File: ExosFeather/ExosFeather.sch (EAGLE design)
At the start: 12 parts, among them J2 TC_2050_IDC_TOP, J6 CONN_2X1_JST_PA, U1 MCP73831, U2 STM32L052KX

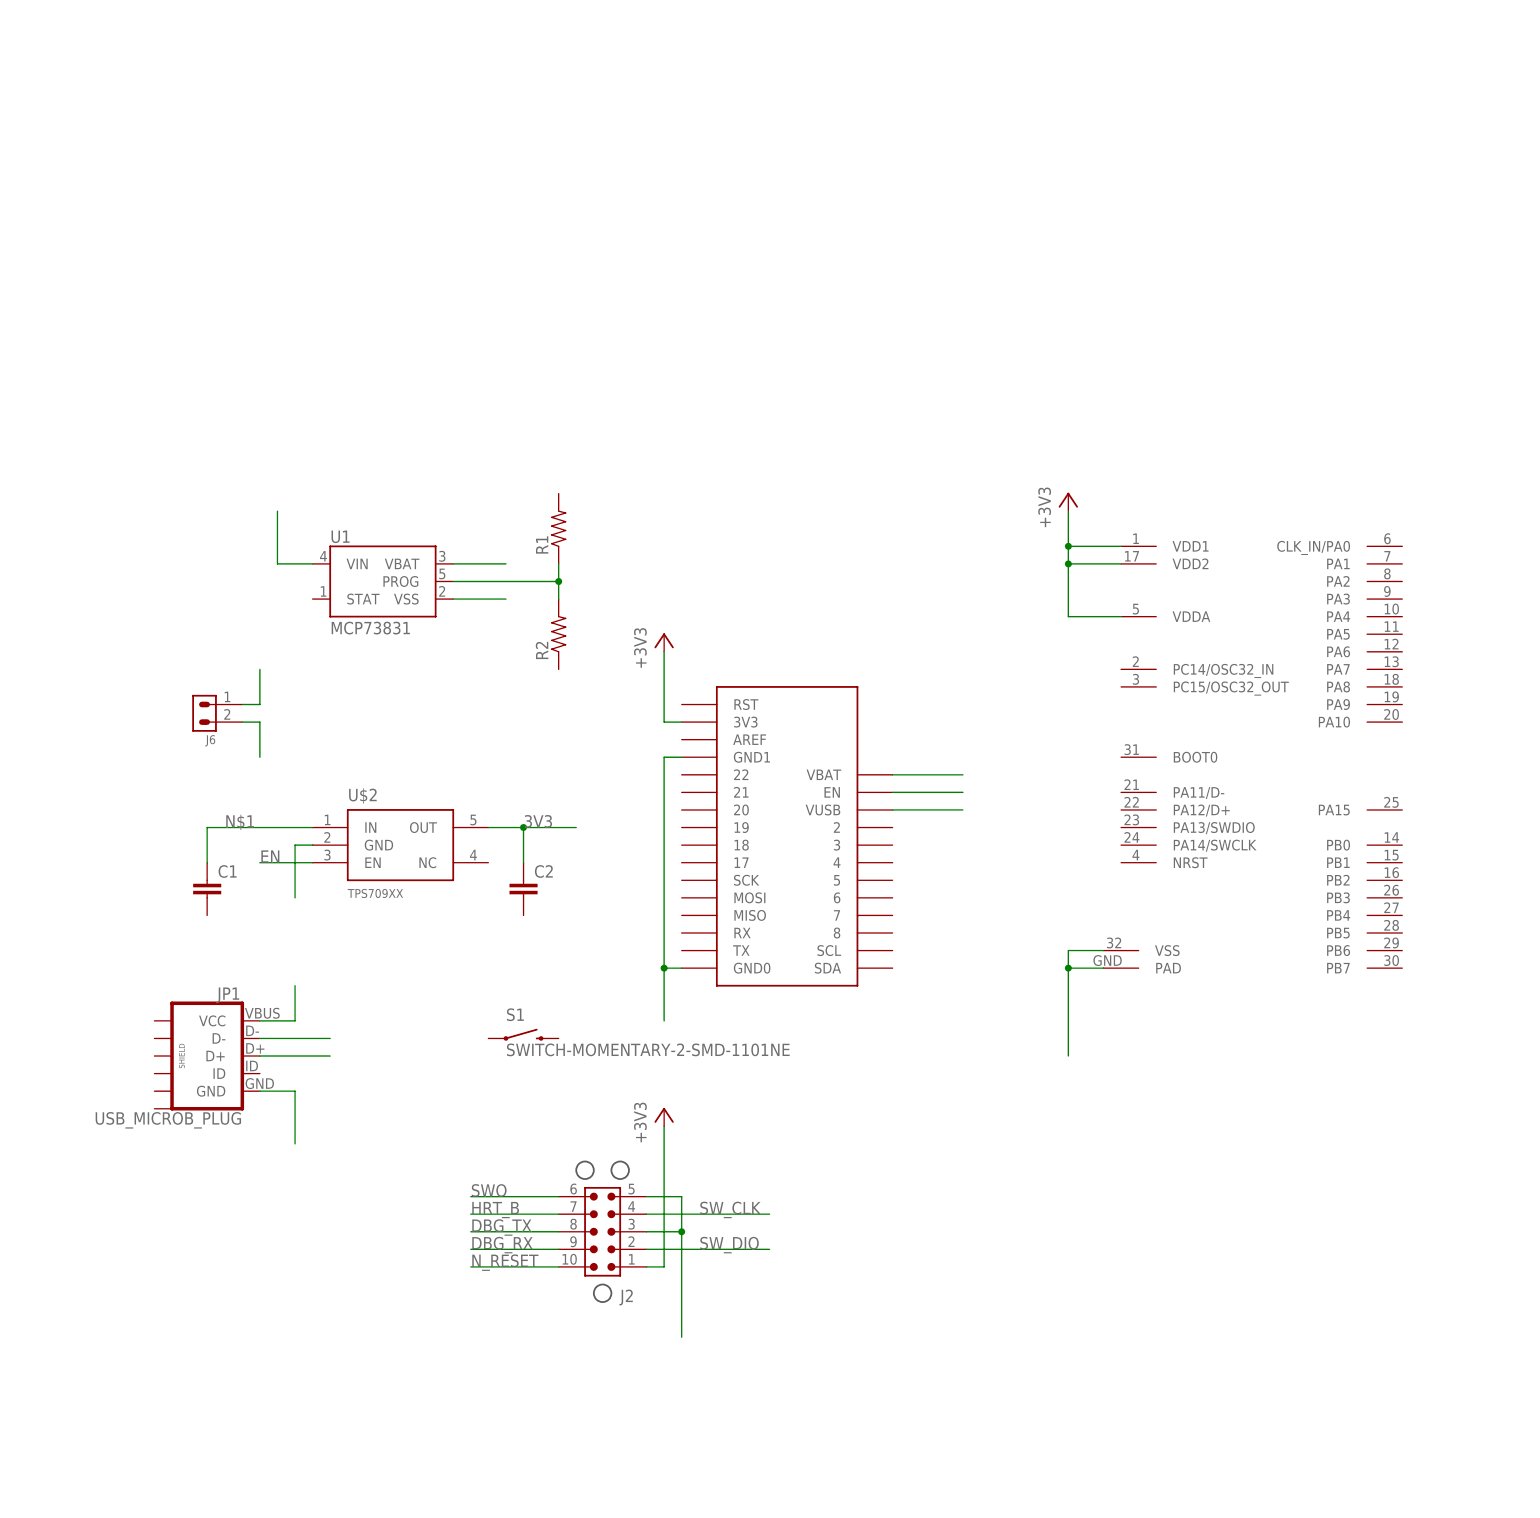
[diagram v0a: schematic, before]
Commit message: exosfeather
updated the pinouts
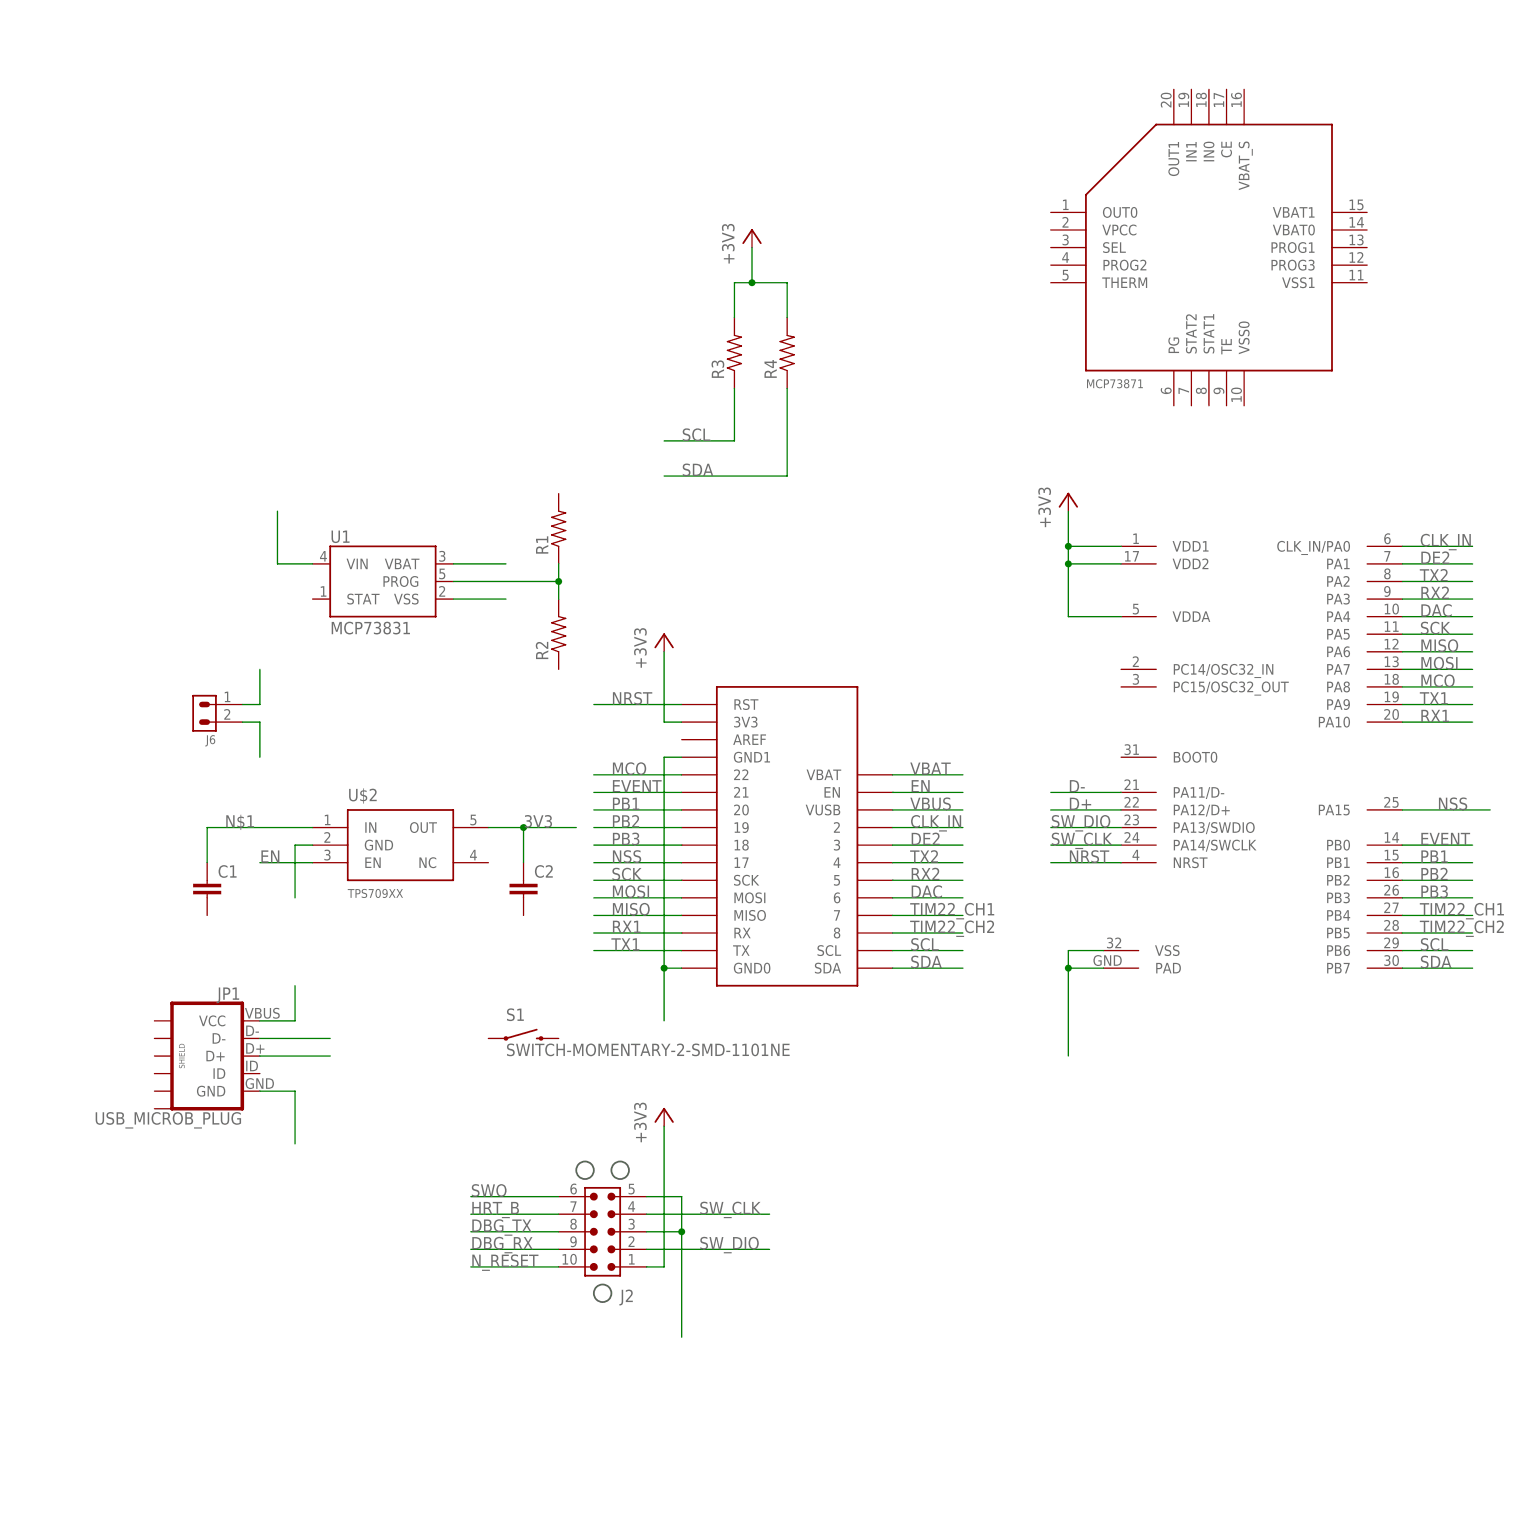
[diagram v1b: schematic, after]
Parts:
- added R3, R4: (no value), stepOSP:0603_RES
- added U$3: MCP73871, stepOSP:MCP73871
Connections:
- new net CLK_IN: U$1.2, U2.CLK_IN/PA0
- new net DAC: U$1.6, U2.PA4
- new net DE2: U$1.3, U2.PA1
- new net EVENT: U$1.21, U2.PB0
- new net MCO: U$1.22, U2.PA8
- new net MISO: U$1.MISO, U2.PA6
- new net MOSI: U$1.MOSI, U2.PA7
- new net NRST: U$1.RST, U2.NRST
- new net NSS: U$1.17, U2.PA15
- new net PB1: U$1.20, U2.PB1
- new net PB2: U$1.19, U2.PB2
- new net PB3: U$1.18, U2.PB3
- new net RX1: U$1.RX, U2.PA10
- new net RX2: U$1.5, U2.PA3
- new net SCK: U$1.SCK, U2.PA5
- new net SCL: R3.1, U$1.SCL, U2.PB6
- new net SDA: R4.1, U$1.SDA, U2.PB7
- new net TIM22_CH1: U$1.7, U2.PB4
- new net TIM22_CH2: U$1.8, U2.PB5
- new net TX1: U$1.TX, U2.PA9
- new net TX2: U$1.4, U2.PA2
- net +3V3: now also R3.2, R4.2
- net D+: now also U2.PA12/D+
- net D-: now also U2.PA11/D-
- net SW_CLK: now also U2.PA14/SWCLK
- net SW_DIO: now also U2.PA13/SWDIO

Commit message: exosfeather
added some new parts
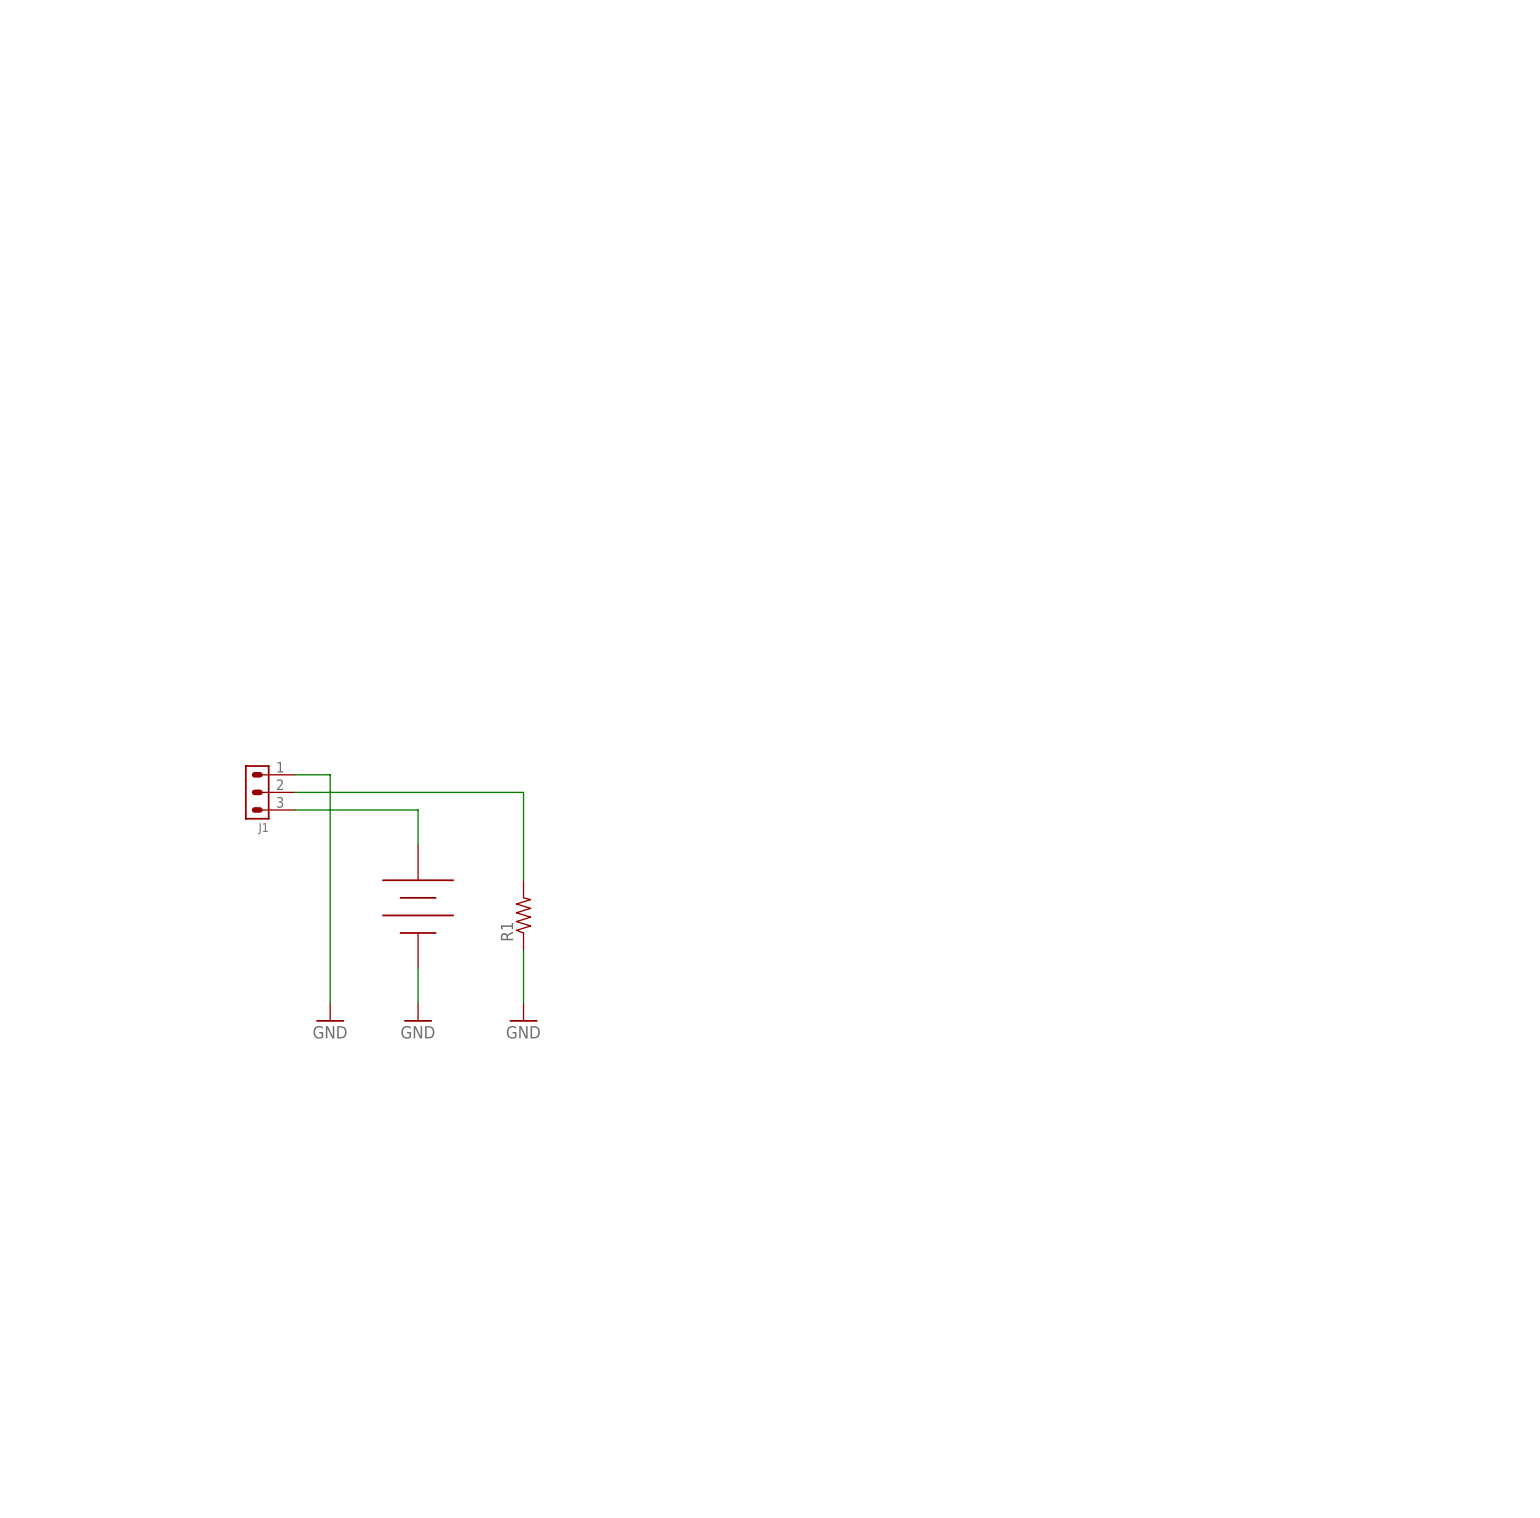
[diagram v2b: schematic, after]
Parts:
- removed C1, C2: (no value), stepOSP:0603_CAP
- removed J2: TC_2050_IDC_TOP, leaf:TC_2050_IDC_TOP
- removed J6: CONN_2X1_JST_PA, leaf:CONN_2X1_JST_PA
- removed JP1: USB_MICROB_PLUG, stepOSP:USB_MICROB_PLUG
- removed R2, R3, R4: (no value), stepOSP:0603_RES
- removed S1: SWITCH-MOMENTARY-2-SMD-1101NE, SparkFun-Electromechanical:SWITCH-MOMENTARY-2-SMD-1101NE
- removed U$1: FEATHER_PINOUT_FULL, stepOSP:FEATHER_PINOUT_FULL
- removed U$3: MCP73871, stepOSP:MCP73871
- removed U1: MCP73831, SparkFun-PowerIC:MCP73831
- removed U2: STM32L052KX, leaf:STM32L052KX
- added J1: CONN_3X1_JST_PA, leaf:CONN_3X1_JST_PA
- U$2: value TPS709XX -> 14500_KEYSTONE_1024; device stepOSP:TPS709XX -> stepOSP:14500_KEYSTONE_1024
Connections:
- removed net +3V3: J2.1, R3.2, R4.2, U$1.3V3, U2.VDD1, U2.VDD2, U2.VDDA
- removed net 3V3: C2.1, U$2.OUT
- removed net CLK_IN: U$1.2, U2.CLK_IN/PA0
- removed net D+: JP1.D+, U2.PA12/D+
- removed net D-: JP1.D-, U2.PA11/D-
- removed net DAC: U$1.6, U2.PA4
- removed net DBG_RX: J2.9
- removed net DBG_TX: J2.8
- removed net DE2: U$1.3, U2.PA1
- removed net EN: U$1.EN, U$2.EN
- removed net EVENT: U$1.21, U2.PB0
- removed net HRT_B: J2.7
- removed net MCO: U$1.22, U2.PA8
- removed net MISO: U$1.MISO, U2.PA6
- removed net MOSI: U$1.MOSI, U2.PA7
- removed net N$3: U1.VIN
- removed net N$4: J6.1
- removed net N$5: R1.1, R2.2, U1.PROG
- removed net N$6: U1.VBAT
- removed net N$7: U1.VSS
- removed net NRST: U$1.RST, U2.NRST
- removed net NSS: U$1.17, U2.PA15
- removed net N_RESET: J2.10
- removed net PB1: U$1.20, U2.PB1
- removed net PB2: U$1.19, U2.PB2
- removed net PB3: U$1.18, U2.PB3
- removed net RX1: U$1.RX, U2.PA10
- removed net RX2: U$1.5, U2.PA3
- removed net SCK: U$1.SCK, U2.PA5
- removed net SCL: R3.1, U$1.SCL, U2.PB6
- removed net SDA: R4.1, U$1.SDA, U2.PB7
- removed net SWO: J2.6
- removed net SW_CLK: J2.4, U2.PA14/SWCLK
- removed net SW_DIO: J2.2, U2.PA13/SWDIO
- removed net TIM22_CH1: U$1.7, U2.PB4
- removed net TIM22_CH2: U$1.8, U2.PB5
- removed net TX1: U$1.TX, U2.PA9
- removed net TX2: U$1.4, U2.PA2
- removed net VBAT: U$1.VBAT
- removed net VBUS: U$1.VUSB
- net GND: now also J1.1, R1.1, U$2.NEG; no longer J2.3, J2.5, J6.2, JP1.GND, U$1.GND0, U$1.GND1, U$2.GND, U2.PAD, U2.VSS
- net N$1: now also J1.2, R1.2; no longer C1.1, U$2.IN
- net N$2: now also J1.3, U$2.POS; no longer JP1.VCC
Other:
- moved on the sheet: R1

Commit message: Revert "exosfeather"
This reverts commit d5dd059b457cfbbf08893ff69975569f2ea8e21c.
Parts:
- removed J1: CONN_3X1_JST_PA, leaf:CONN_3X1_JST_PA
- added C1, C2: (no value), stepOSP:0603_CAP
- added J2: TC_2050_IDC_TOP, leaf:TC_2050_IDC_TOP
- added J6: CONN_2X1_JST_PA, leaf:CONN_2X1_JST_PA
- added JP1: USB_MICROB_PLUG, stepOSP:USB_MICROB_PLUG
- added R2, R3, R4: (no value), stepOSP:0603_RES
- added S1: SWITCH-MOMENTARY-2-SMD-1101NE, SparkFun-Electromechanical:SWITCH-MOMENTARY-2-SMD-1101NE
- added U$1: FEATHER_PINOUT_FULL, stepOSP:FEATHER_PINOUT_FULL
- added U$3: MCP73871, stepOSP:MCP73871
- added U1: MCP73831, SparkFun-PowerIC:MCP73831
- added U2: STM32L052KX, leaf:STM32L052KX
- U$2: value 14500_KEYSTONE_1024 -> TPS709XX; device stepOSP:14500_KEYSTONE_1024 -> stepOSP:TPS709XX
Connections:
- new net +3V3: J2.1, R3.2, R4.2, U$1.3V3, U2.VDD1, U2.VDD2, U2.VDDA
- new net 3V3: C2.1, U$2.OUT
- new net CLK_IN: U$1.2, U2.CLK_IN/PA0
- new net D+: JP1.D+, U2.PA12/D+
- new net D-: JP1.D-, U2.PA11/D-
- new net DAC: U$1.6, U2.PA4
- new net DBG_RX: J2.9
- new net DBG_TX: J2.8
- new net DE2: U$1.3, U2.PA1
- new net EN: U$1.EN, U$2.EN
- new net EVENT: U$1.21, U2.PB0
- new net HRT_B: J2.7
- new net MCO: U$1.22, U2.PA8
- new net MISO: U$1.MISO, U2.PA6
- new net MOSI: U$1.MOSI, U2.PA7
- new net N$3: U1.VIN
- new net N$4: J6.1
- new net N$5: R1.1, R2.2, U1.PROG
- new net N$6: U1.VBAT
- new net N$7: U1.VSS
- new net NRST: U$1.RST, U2.NRST
- new net NSS: U$1.17, U2.PA15
- new net N_RESET: J2.10
- new net PB1: U$1.20, U2.PB1
- new net PB2: U$1.19, U2.PB2
- new net PB3: U$1.18, U2.PB3
- new net RX1: U$1.RX, U2.PA10
- new net RX2: U$1.5, U2.PA3
- new net SCK: U$1.SCK, U2.PA5
- new net SCL: R3.1, U$1.SCL, U2.PB6
- new net SDA: R4.1, U$1.SDA, U2.PB7
- new net SWO: J2.6
- new net SW_CLK: J2.4, U2.PA14/SWCLK
- new net SW_DIO: J2.2, U2.PA13/SWDIO
- new net TIM22_CH1: U$1.7, U2.PB4
- new net TIM22_CH2: U$1.8, U2.PB5
- new net TX1: U$1.TX, U2.PA9
- new net TX2: U$1.4, U2.PA2
- new net VBAT: U$1.VBAT
- new net VBUS: U$1.VUSB
- net GND: now also J2.3, J2.5, J6.2, JP1.GND, U$1.GND0, U$1.GND1, U$2.GND, U2.PAD, U2.VSS; no longer J1.1, R1.1, U$2.NEG
- net N$1: now also C1.1, U$2.IN; no longer J1.2, R1.2
- net N$2: now also JP1.VCC; no longer J1.3, U$2.POS
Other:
- moved on the sheet: R1

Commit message: exofeather update
latest and greates exofeather
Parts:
- removed U$3: MCP73871, stepOSP:MCP73871
- added C3, C4: (no value), stepOSP:0603_CAP
- added D1: 0603_LED, stepOSP:0603_LED
- added J1: JST_PH_2_PTH, stepOSP:JST_PH_2_PTH
- added R5: (no value), stepOSP:0603_RES
- added U$17: TC_2050_IDC_TOP, leaf:TC_2050_IDC_TOP
- added U3: TI_CHGR_BQ21040, leaf:TI_CHGR_BQ21040
- U1: value MCP73831 -> TVS_USB_TPD4S012; device SparkFun-PowerIC:MCP73831 -> leaf:TVS_USB_TPD4S012
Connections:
- removed net 3V3: C2.1, U$2.OUT
- removed net DBG_RX: J2.9
- removed net DBG_TX: J2.8
- removed net HRT_B: J2.7
- removed net N$1: C1.1, U$2.IN
- removed net N$2: JP1.VCC
- removed net N$4: J6.1
- net +3V3: now also C2.1, U$2.OUT
- net D+: now also U1.D+
- net D-: now also U1.D-
- net GND: now also C1.2, C2.2, C3.2, C4.2, J6.1, R1.1, R2.2, U1.GND, U3.GND; no longer J6.2
- net MCO: now also J2.7
- net N$3: now also J1.2, R2.1, U3.TS; no longer U1.VIN
- net N$5: now also R1.2, U3.ISET; no longer R1.1, R2.2, U1.PROG
- net N$6: now also D1.C, U3.NCHG; no longer U1.VBAT
- net N$7: now also D1.A, R5.1; no longer U1.VSS
- net RX1: now also J2.9
- net TX1: now also J2.8
- net VBAT: now also C1.1, C4.1, J6.2, R5.2, U$2.IN, U3.OUT
- net VBUS: now also C3.1, JP1.VCC, U1.VBUS, U3.VIN
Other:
- moved on the sheet: C1, C2, J2, J6, R1, R2, R3, R4, U$2
